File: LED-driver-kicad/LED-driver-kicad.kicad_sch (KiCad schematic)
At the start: 38 parts, among them SW1 SW_SPST, U1 ARJM11C7-114-BA-EW2, U2 NCP1095DBR2, U4 25AA02E64-I/SN, U5 PIC18F97J60-IPF, Y1 25MHz

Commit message: add separate hierarchical sheets for ethernet and main microcontroller
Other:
- added sheet Ethernet (Ethernet.kicad_sch)
- added sheet Microcontroller (Microcontroller.kicad_sch)
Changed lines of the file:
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@@
+    )
+  )
+  (sheet (at 307.34 34.29) (size 25.4 19.05) (fields_autoplaced)
+    (stroke (width 0.1524) (type solid))
+    (fill (color 0 0 0 0.0000))
+    (property "Sheetname" "Ethernet" (at 307.34 33.5784 0)
+      (effects (font (size 1.27 1.27)) (justify left bottom))
+    )
+    (property "Sheetfile" "Ethernet.kicad_sch" (at 307.34 53.9246 0)
+      (effects (font (size 1.27 1.27)) (justify left top))
+    )
+    (instances
+      (project "LED-driver-kicad"
+        (path "/2b071084-2ab6-4896-84cc-45b211479417" (page "3"))
+      )
+    )
+  )
+  (sheet (at 342.9 36.83) (size 24.13 19.05) (fields_autoplaced)
+    (stroke (width 0.1524) (type solid))
+    (fill (color 0 0 0 0.0000))
+    (property "Sheetname" "Microcontroller" (at 342.9 36.1184 0)
+      (effects (font (size 1.27 1.27)) (justify left bottom))
+    )
+    (property "Sheetfile" "Microcontroller.kicad_sch" (at 342.9 56.4646 0)
+      (effects (font (size 1.27 1.27)) (justify left top))
+    )
+    (instances
+      (project "LED-driver-kicad"
+        (path "/2b071084-2ab6-4896-84cc-45b211479417" (page "4"))
+      )
     )
   )

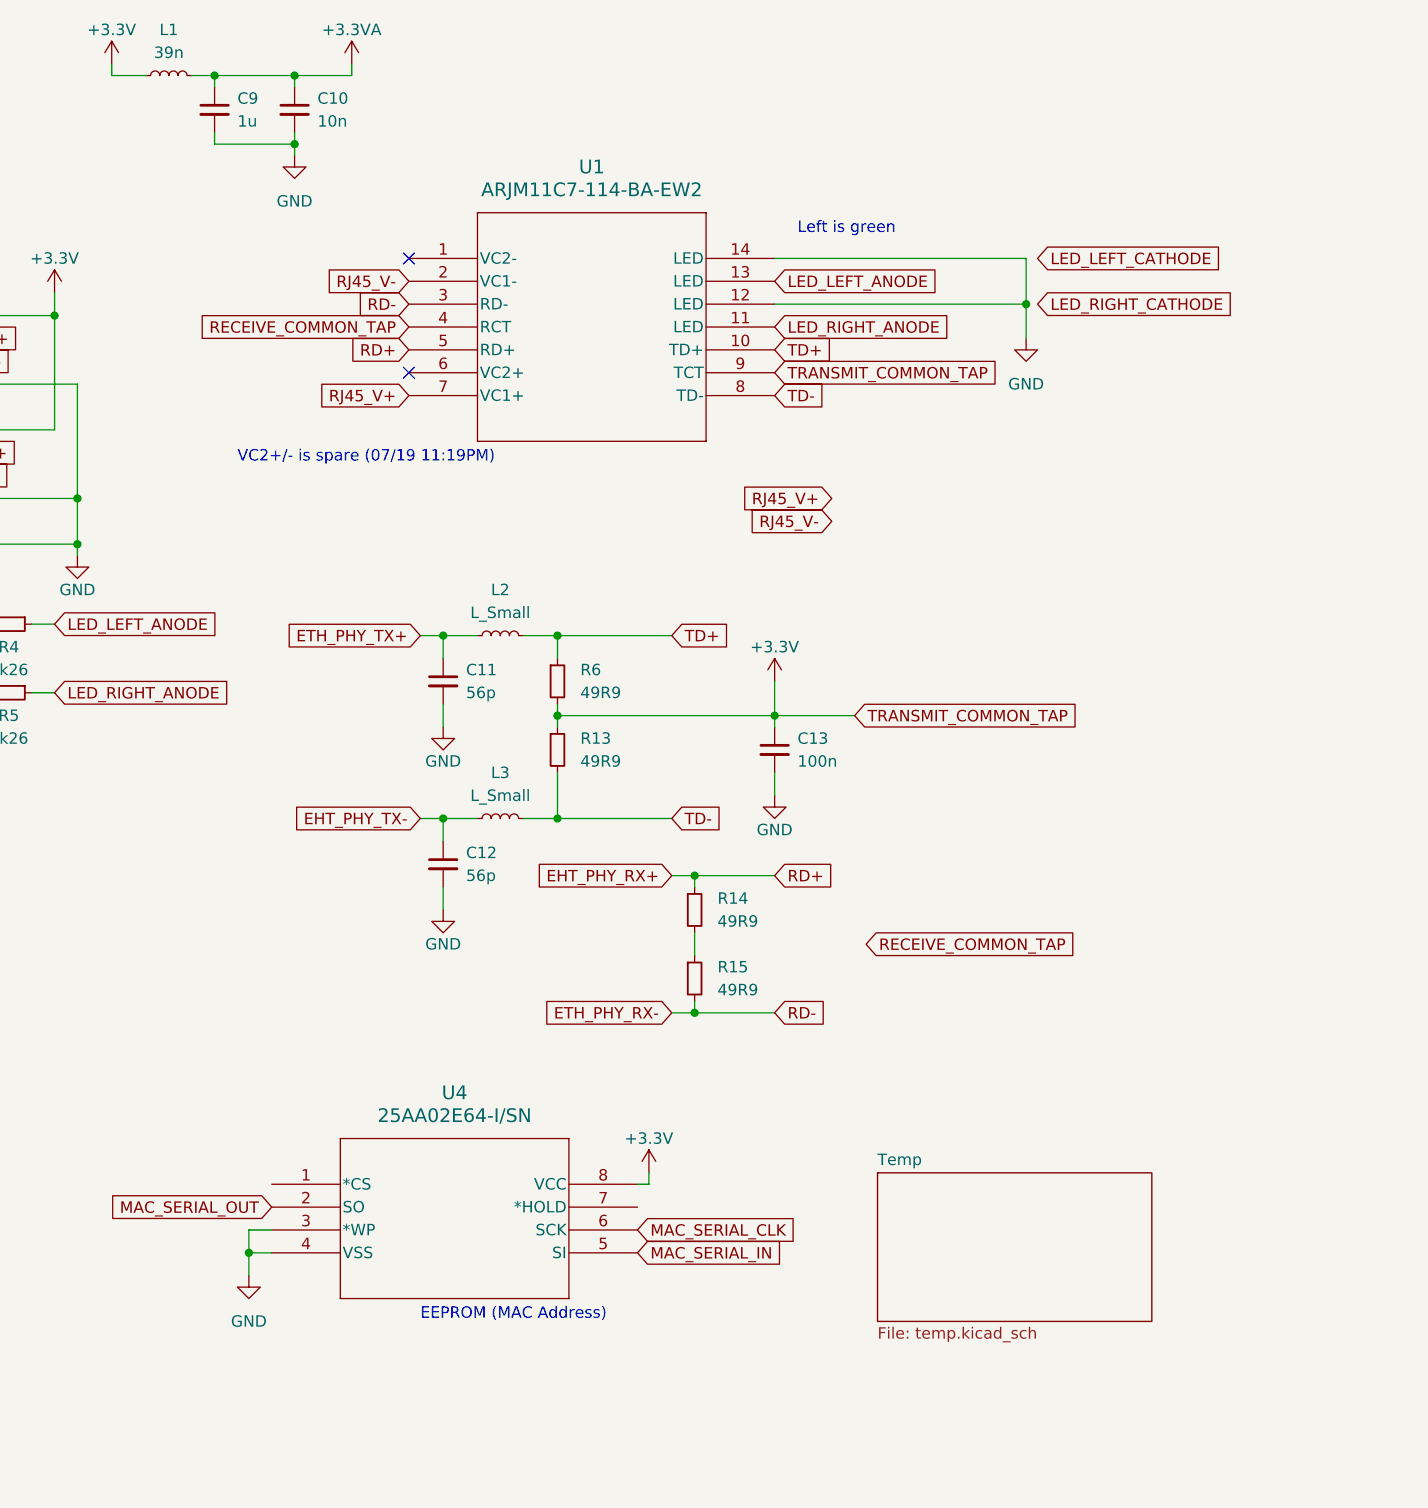
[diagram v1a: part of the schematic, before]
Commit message: delete Temp schematic sheet
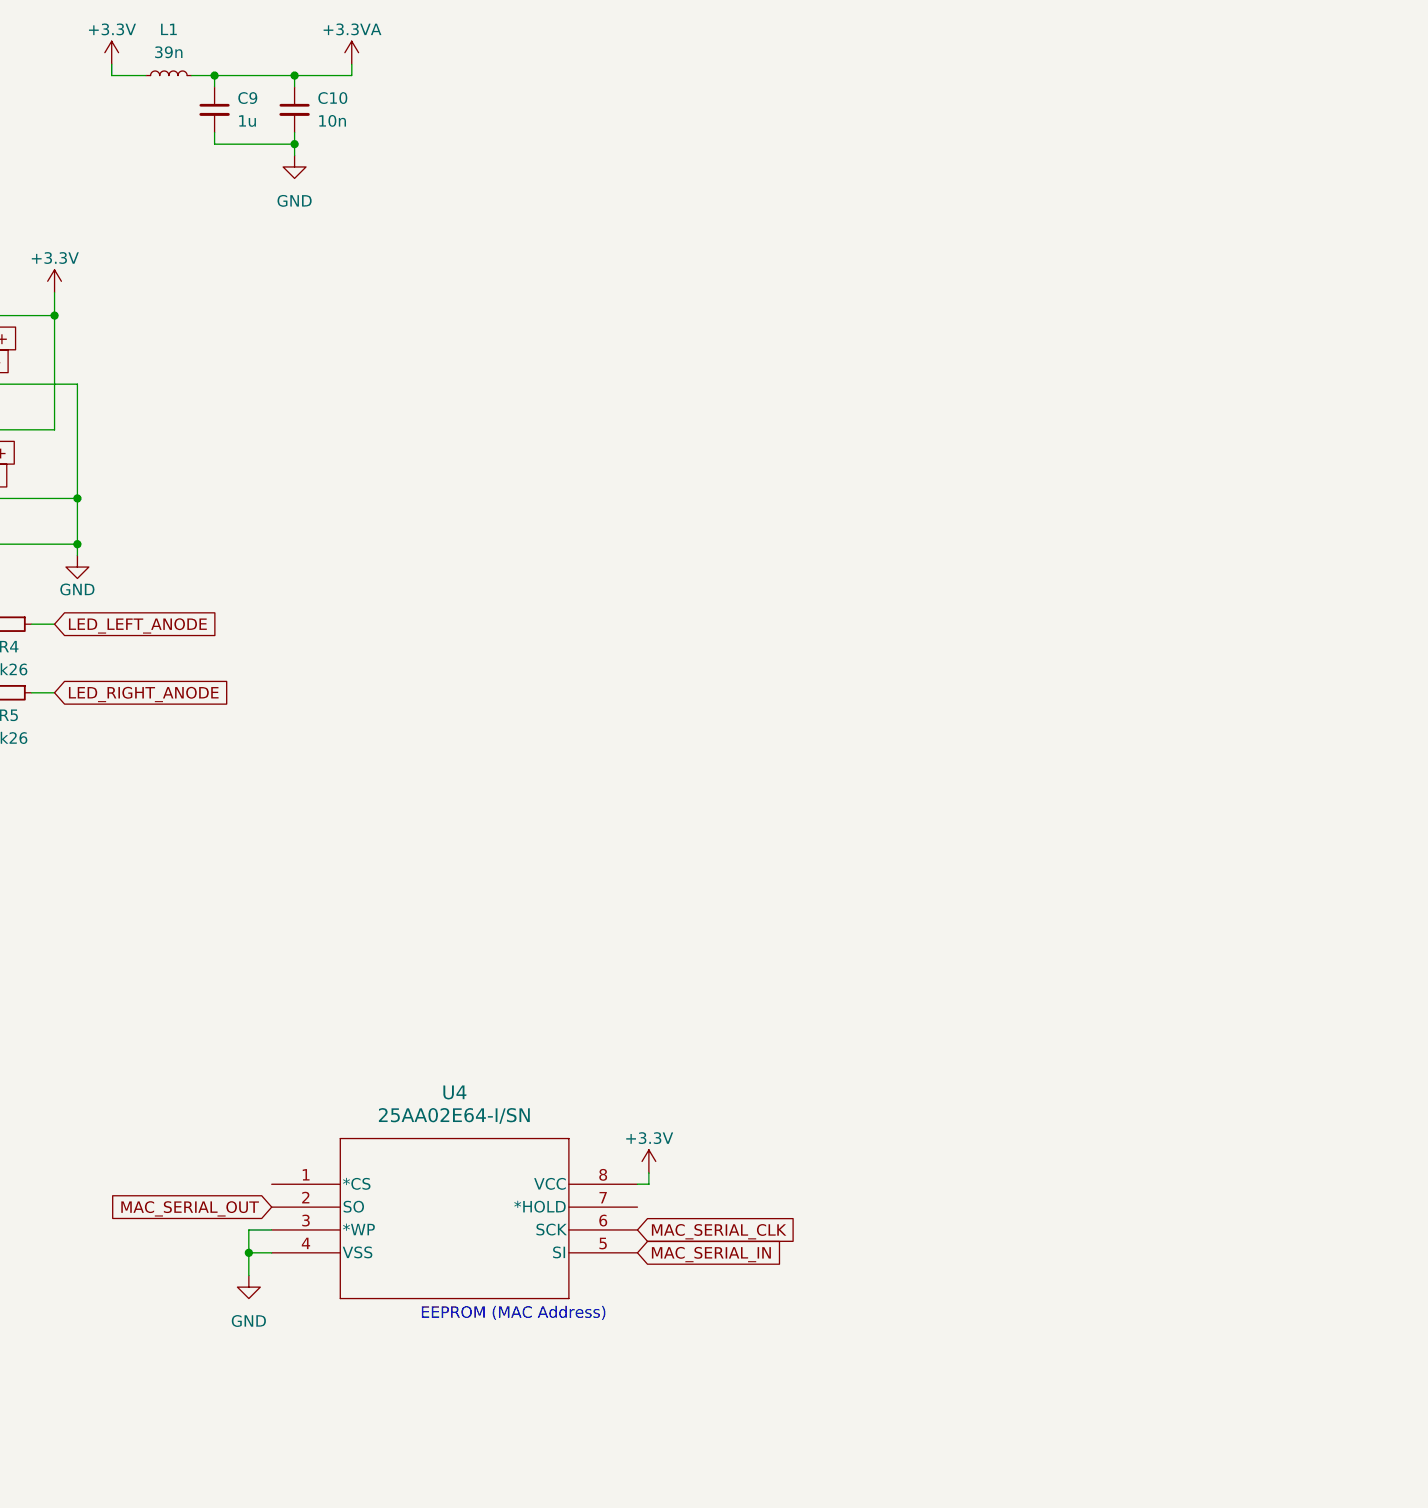
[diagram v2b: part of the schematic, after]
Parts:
- removed C11, C12: 56p, symbol Device:C_Small
- removed C13: 100n, symbol Device:C_Small
- removed L2, L3: L_Small, symbol Device:L_Small
- removed R13, R14, R15, R6: 49R9, symbol Device:R_Small
- removed U1: ARJM11C7-114-BA-EW2, ARJM11C7-114-BA-EW2_ABR, symbol ARJM11C7-114-BA-EW2:ARJM11C7-114-BA-EW2
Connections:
- no-connect marks 2 -> 0
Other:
- removed sheet Temp
- note removed: "Left is green"
- note removed: "VC2+/- is spare (07/19 11:19PM)"
